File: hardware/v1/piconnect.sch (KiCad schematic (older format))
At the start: 6 parts

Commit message: Some autorouting on 16led row
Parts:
- P1, P2, P3, P4, P5, P6: renamed from P?; footprint (none) -> Pin_Headers:Pin_Header_Angled_2x05
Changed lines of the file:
@@
 Connection ~ 6150 1850
 $Comp
-L VCC #PWR?
+L VCC #PWR01
 U 1 1 57A60478
 P 3350 700
-F 0 "#PWR?" H 3350 550 50  0001 C CNN
+F 0 "#PWR01" H 3350 550 50  0001 C CNN
 F 1 "VCC" H 3350 850 50  0000 C CNN
 F 2 "" H 3350 700 50  0000 C CNN
@@
 $EndComp
 $Comp
-L VDD #PWR?
+L VDD #PWR02
 U 1 1 57A60684
 P 2950 700
-F 0 "#PWR?" H 2950 550 50  0001 C CNN
+F 0 "#PWR02" H 2950 550 50  0001 C CNN
 F 1 "VDD" H 2950 850 50  0000 C CNN
 F 2 "" H 2950 700 50  0000 C CNN
@@
 NoConn ~ 6800 4900
 $Comp
-L VCC #PWR?
+L VCC #PWR03
 U 1 1 57A68689
 P 6650 1150
-F 0 "#PWR?" H 6650 1000 50  0001 C CNN
+F 0 "#PWR03" H 6650 1000 50  0001 C CNN
 F 1 "VCC" H 6650 1300 50  0000 C CNN
 F 2 "" H 6650 1150 50  0000 C CNN
@@
 $EndComp
 $Comp
-L VCC #PWR?
+L VCC #PWR04
 U 1 1 57A687E4
 P 6650 4000
-F 0 "#PWR?" H 6650 3850 50  0001 C CNN
+F 0 "#PWR04" H 6650 3850 50  0001 C CNN
 F 1 "VCC" H 6650 4150 50  0000 C CNN
 F 2 "" H 6650 4000 50  0000 C CNN
@@
 	6650 1250 6650 1150
 $Comp
-L GND #PWR?
+L GND #PWR05
 U 1 1 57A68AD3
 P 6650 1400
-F 0 "#PWR?" H 6650 1150 50  0001 C CNN
+F 0 "#PWR05" H 6650 1150 50  0001 C CNN
 F 1 "GND" H 6650 1250 50  0000 C CNN
 F 2 "" H 6650 1400 50  0000 C CNN
@@
 	6800 1400 6650 1400
 $Comp
-L GND #PWR?
+L GND #PWR06
 U 1 1 57A691A3
 P 6700 4300
-F 0 "#PWR?" H 6700 4050 50  0001 C CNN
+F 0 "#PWR06" H 6700 4050 50  0001 C CNN
 F 1 "GND" H 6700 4150 50  0000 C CNN
 F 2 "" H 6700 4300 50  0000 C CNN
@@
 	7900 4250 8000 4250
 $Comp
-L CONN_02X05 P?
+L CONN_02X05 P1
 U 1 1 57A6EF47
 P 9900 1500
-F 0 "P?" H 9900 1800 50  0000 C CNN
+F 0 "P1" H 9900 1800 50  0000 C CNN
 F 1 "CONN_02X05" H 9900 1200 50  0000 C CNN
-F 2 "" H 9900 300 50  0000 C CNN
+F 2 "Pin_Headers:Pin_Header_Angled_2x05" H 9900 300 50  0001 C CNN
 F 3 "" H 9900 300 50  0000 C CNN
 	1    9900 1500
@@
 A_DIG1
 $Comp
-L CONN_02X05 P?
+L CONN_02X05 P2
 U 1 1 57A709A7
 P 9900 2250
-F 0 "P?" H 9900 2550 50  0000 C CNN
+F 0 "P2" H 9900 2550 50  0000 C CNN
 F 1 "CONN_02X05" H 9900 1950 50  0000 C CNN
-F 2 "" H 9900 1050 50  0000 C CNN
+F 2 "Pin_Headers:Pin_Header_Angled_2x05" H 9900 1050 50  0001 C CNN
 F 3 "" H 9900 1050 50  0000 C CNN
 	1    9900 2250
@@
 A_DIG3
 $Comp
-L CONN_02X05 P?
+L CONN_02X05 P3
 U 1 1 57A70B37
 P 9900 3000
-F 0 "P?" H 9900 3300 50  0000 C CNN
+F 0 "P3" H 9900 3300 50  0000 C CNN
 F 1 "CONN_02X05" H 9900 2700 50  0000 C CNN
-F 2 "" H 9900 1800 50  0000 C CNN
+F 2 "Pin_Headers:Pin_Header_Angled_2x05" H 9900 1800 50  0001 C CNN
 F 3 "" H 9900 1800 50  0000 C CNN
 	1    9900 3000
@@
 A_DIG5
 $Comp
-L CONN_02X05 P?
+L CONN_02X05 P4
 U 1 1 57A7120E
 P 9900 3700
-F 0 "P?" H 9900 4000 50  0000 C CNN
+F 0 "P4" H 9900 4000 50  0000 C CNN
 F 1 "CONN_02X05" H 9900 3400 50  0000 C CNN
-F 2 "" H 9900 2500 50  0000 C CNN
+F 2 "Pin_Headers:Pin_Header_Angled_2x05" H 9900 2500 50  0001 C CNN
 F 3 "" H 9900 2500 50  0000 C CNN
 	1    9900 3700
@@
 A_DIG7
 $Comp
-L CONN_02X05 P?
+L CONN_02X05 P5
 U 1 1 57A720A7
 P 9900 4700
-F 0 "P?" H 9900 5000 50  0000 C CNN
+F 0 "P5" H 9900 5000 50  0000 C CNN
 F 1 "CONN_02X05" H 9900 4400 50  0000 C CNN
-F 2 "" H 9900 3500 50  0000 C CNN
+F 2 "Pin_Headers:Pin_Header_Angled_2x05" H 9900 3500 50  0001 C CNN
 F 3 "" H 9900 3500 50  0000 C CNN
 	1    9900 4700
@@
 B_DIG1
 $Comp
-L CONN_02X05 P?
+L CONN_02X05 P6
 U 1 1 57A720B7
 P 9900 5450
-F 0 "P?" H 9900 5750 50  0000 C CNN
+F 0 "P6" H 9900 5750 50  0000 C CNN
 F 1 "CONN_02X05" H 9900 5150 50  0000 C CNN
-F 2 "" H 9900 4250 50  0000 C CNN
+F 2 "Pin_Headers:Pin_Header_Angled_2x05" H 9900 4250 50  0001 C CNN
 F 3 "" H 9900 4250 50  0000 C CNN
 	1    9900 5450

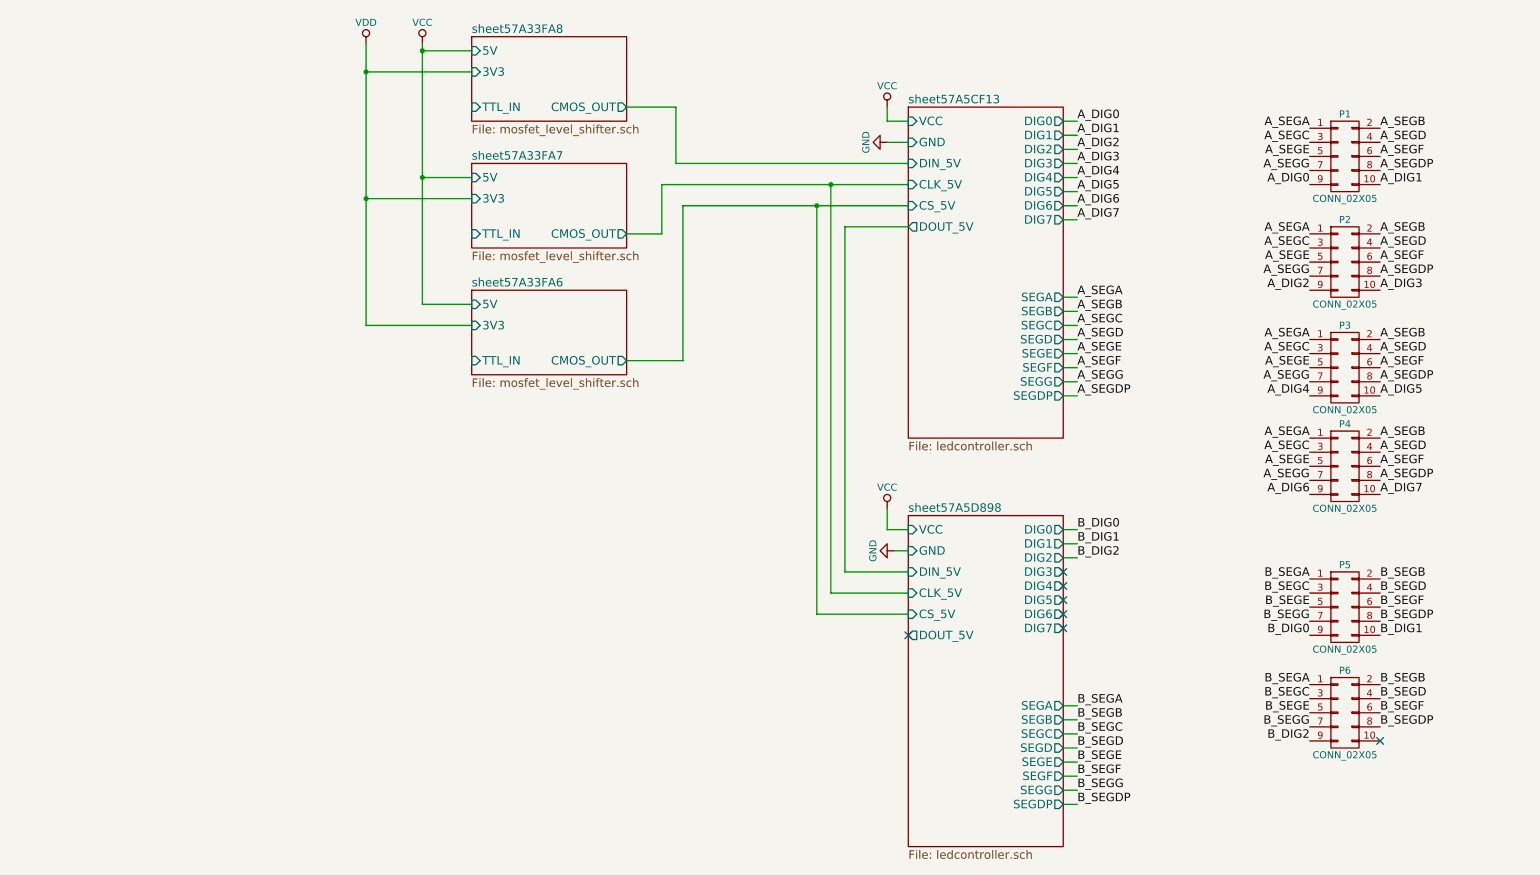
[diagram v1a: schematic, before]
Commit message: Correct lamps-16 connector layout in piconnect board.
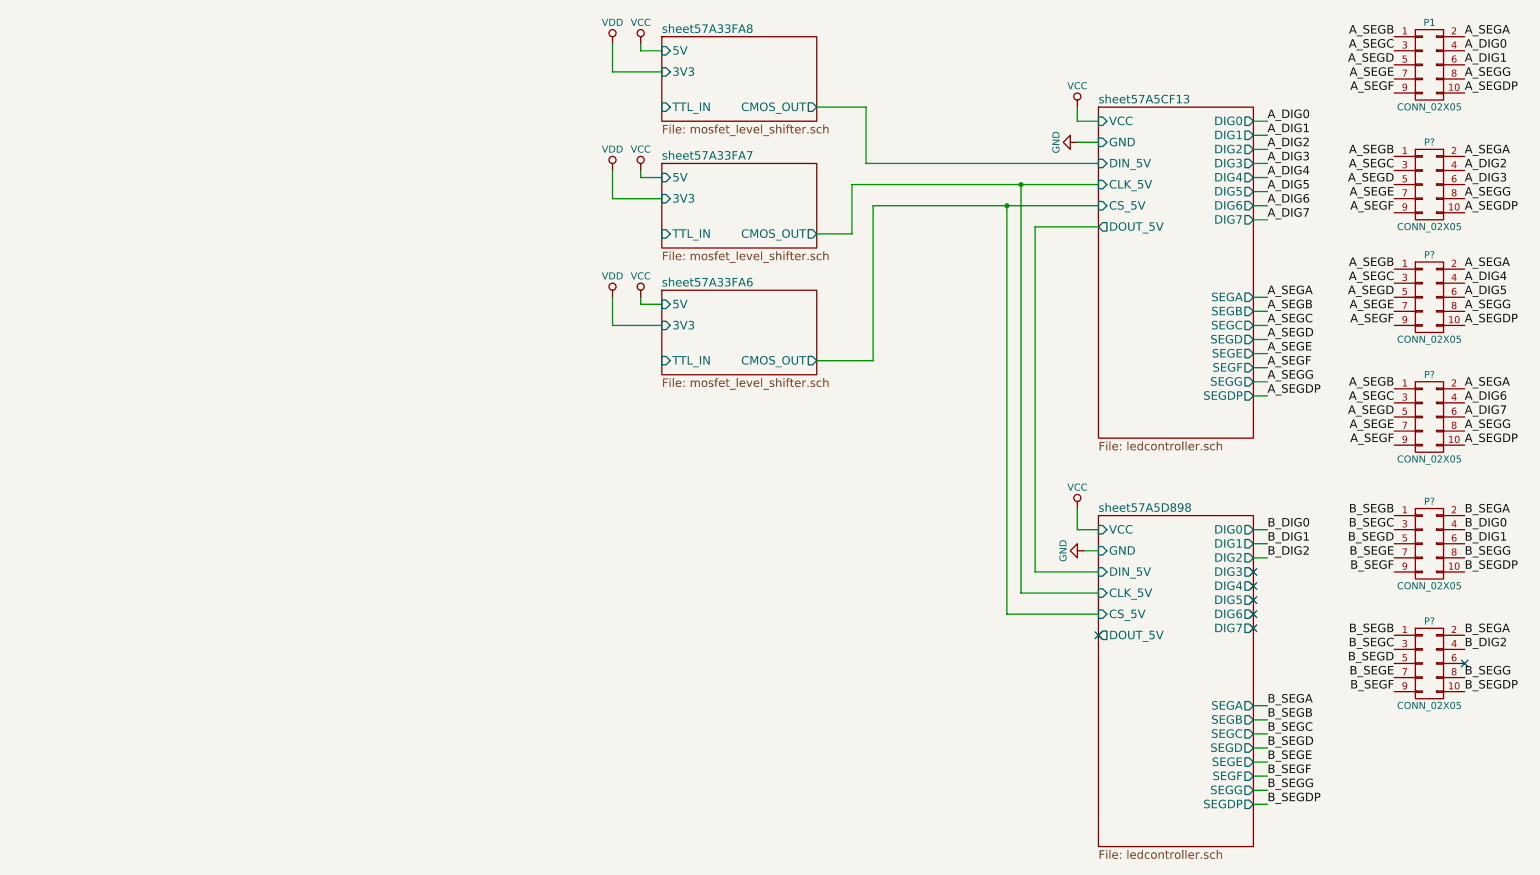
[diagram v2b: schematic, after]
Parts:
- removed P2, P3, P4, P5, P6: CONN_02X05, Pin_Headers:Pin_Header_Angled_2x05, symbol CONN_02X05
- added P? (x5): CONN_02X05, Pin_Headers:Pin_Header_Angled_2x05, symbol CONN_02X05
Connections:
- net A_DIG0: now also P1.4 (P4); no longer P1.9 (P9)
- net A_DIG1: now also P1.6 (P6); no longer P1.10 (P10)
- net A_DIG2: now also P?.4 (P4)
- net A_DIG3: now also P?.6 (P6)
- net A_DIG4: now also P?.4 (P4)
- net A_DIG5: now also P?.6 (P6)
- net A_DIG6: now also P?.4 (P4)
- net A_DIG7: now also P?.6 (P6)
- net A_SEGA: now also P1.2 (P2), P?.2 (P2), P?.2 (P2), P?.2 (P2); no longer P1.1 (P1)
- net A_SEGB: now also P1.1 (P1), P?.1 (P1), P?.1 (P1), P?.1 (P1); no longer P1.2 (P2)
- net A_SEGC: now also P?.3 (P3), P?.3 (P3), P?.3 (P3)
- net A_SEGD: now also P1.5 (P5), P?.5 (P5), P?.5 (P5), P?.5 (P5); no longer P1.4 (P4)
- net A_SEGDP: now also P1.10 (P10), P?.10 (P10), P?.10 (P10), P?.10 (P10); no longer P1.8 (P8)
- net A_SEGE: now also P1.7 (P7), P?.7 (P7), P?.7 (P7), P?.7 (P7); no longer P1.5 (P5)
- net A_SEGF: now also P1.9 (P9), P?.9 (P9), P?.9 (P9), P?.9 (P9); no longer P1.6 (P6)
- net A_SEGG: now also P1.8 (P8), P?.8 (P8), P?.8 (P8), P?.8 (P8); no longer P1.7 (P7)
- net B_DIG0: now also P?.4 (P4)
- net B_DIG1: now also P?.6 (P6)
- net B_DIG2: now also P?.4 (P4)
- net B_SEGA: now also P?.2 (P2), P?.2 (P2)
- net B_SEGB: now also P?.1 (P1), P?.1 (P1)
- net B_SEGC: now also P?.3 (P3), P?.3 (P3)
- net B_SEGD: now also P?.5 (P5), P?.5 (P5)
- net B_SEGDP: now also P?.10 (P10), P?.10 (P10)
- net B_SEGE: now also P?.7 (P7), P?.7 (P7)
- net B_SEGF: now also P?.9 (P9), P?.9 (P9)
- net B_SEGG: now also P?.8 (P8), P?.8 (P8)
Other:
- moved on the sheet: P1

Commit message: Start adding pi gpio port to piconnect board.
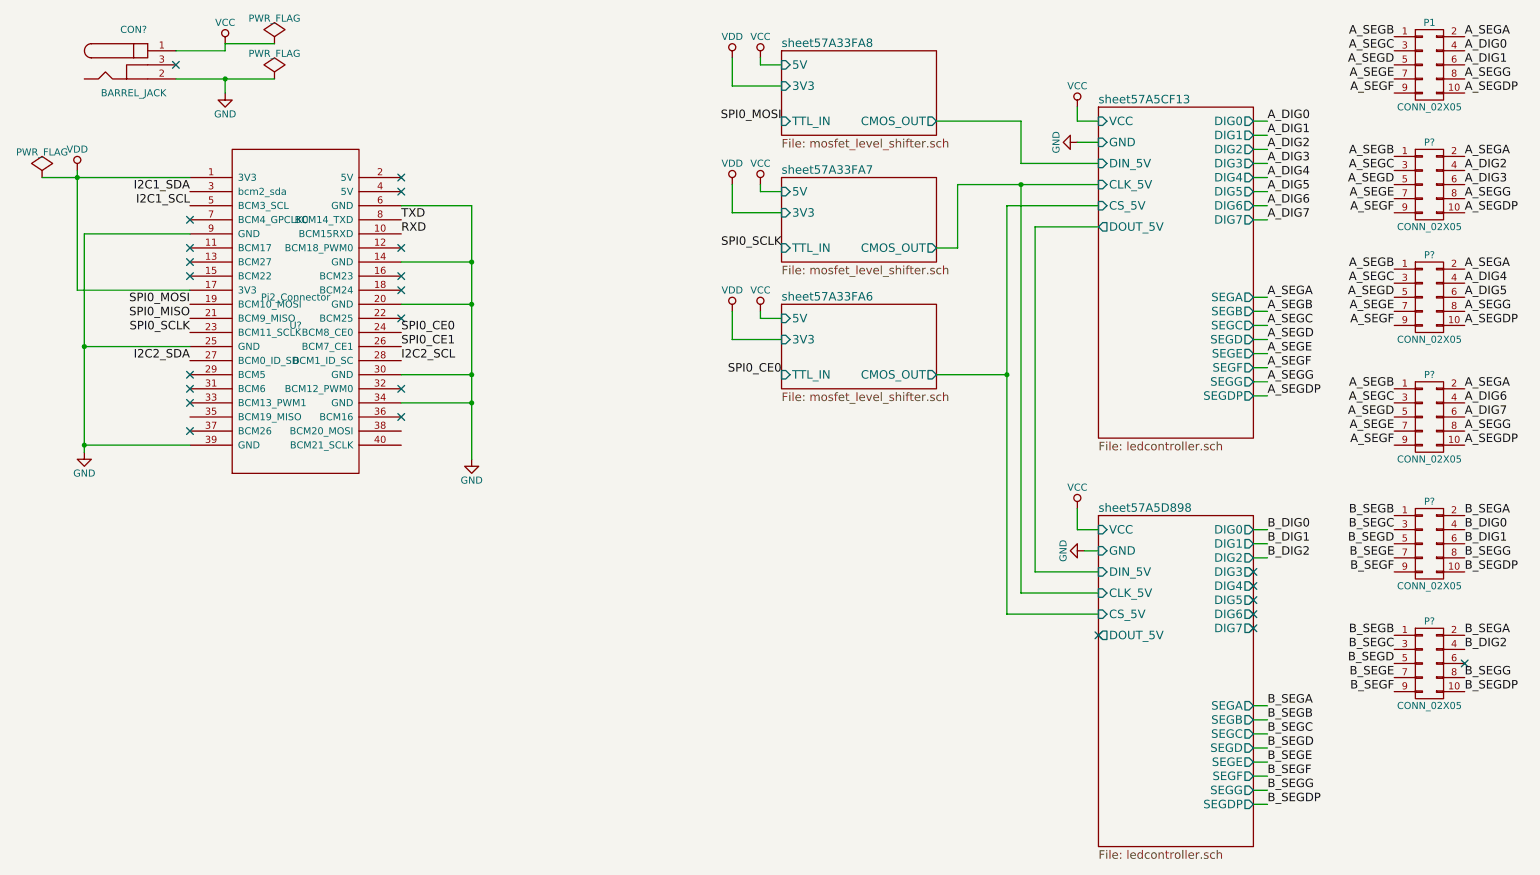
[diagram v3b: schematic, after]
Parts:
- added CON?: BARREL_JACK, symbol BARREL_JACK
- added U?: Pi2_Connector, MODULE, symbol Pi2_Connector
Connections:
- net GND: now also CON?.2, U?.14 (GND), U?.20 (GND), U?.25 (GND), U?.30 (GND), U?.34 (GND), U?.39 (GND), U?.6 (GND), U?.9 (GND)
- net VCC: now also CON?.1
- net VDD: now also U?.1 (3V3), U?.17 (3V3)
- new net I2C1_SCL: U?.5 (BCM3_SCL)
- new net I2C1_SDA: U?.3 (bcm2_sda)
- new net I2C2_SCL: U?.28 (BCM1_ID_SC)
- new net I2C2_SDA: U?.27 (BCM0_ID_SD)
- new net RXD: U?.10 (BCM15RXD)
- new net SPI0_CE0: U?.24 (BCM8_CE0)
- new net SPI0_CE1: U?.26 (BCM7_CE1)
- new net SPI0_MISO: U?.21 (BCM9_MISO)
- new net SPI0_MOSI: U?.19 (BCM10_MOSI)
- new net SPI0_SCLK: U?.23 (BCM11_SCLK)
- new net TXD: U?.8 (BCM14_TXD)
- no-connect marks 7 -> 24
